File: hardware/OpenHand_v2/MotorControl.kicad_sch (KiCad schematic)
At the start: 52 parts, among them U10 DRV8833PWP, U7 DRV8833PWP, U8 DRV8833PWP, U9 DRV8833PWP

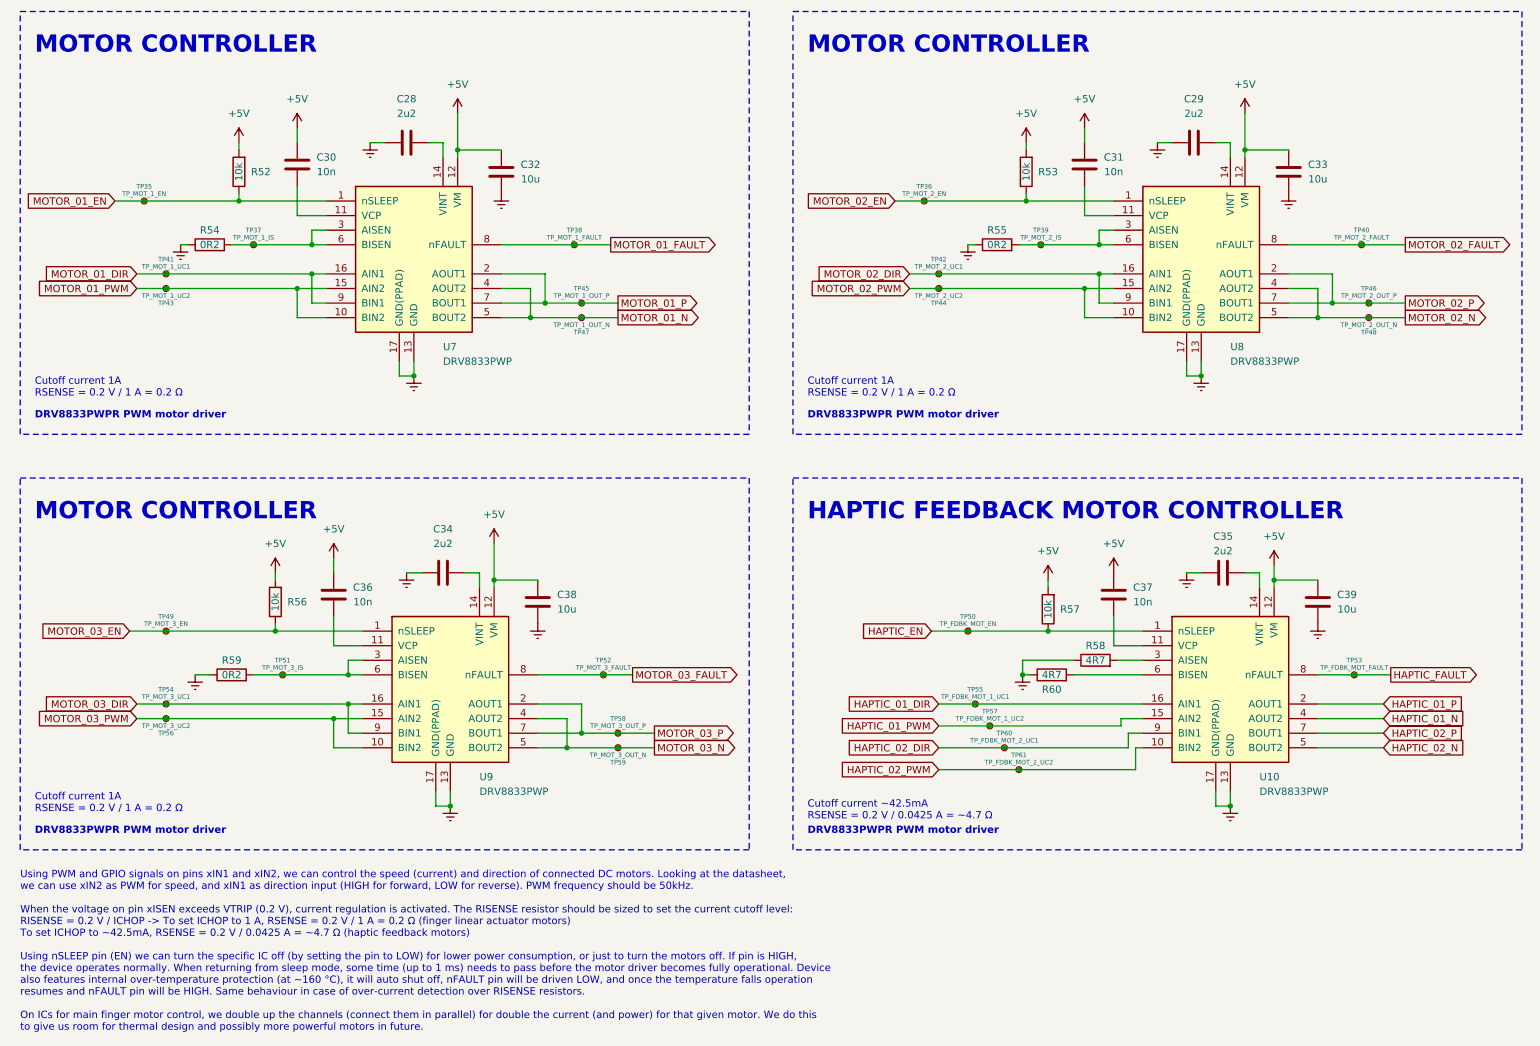
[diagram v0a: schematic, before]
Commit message: Update V2 schematic and start PCB layout
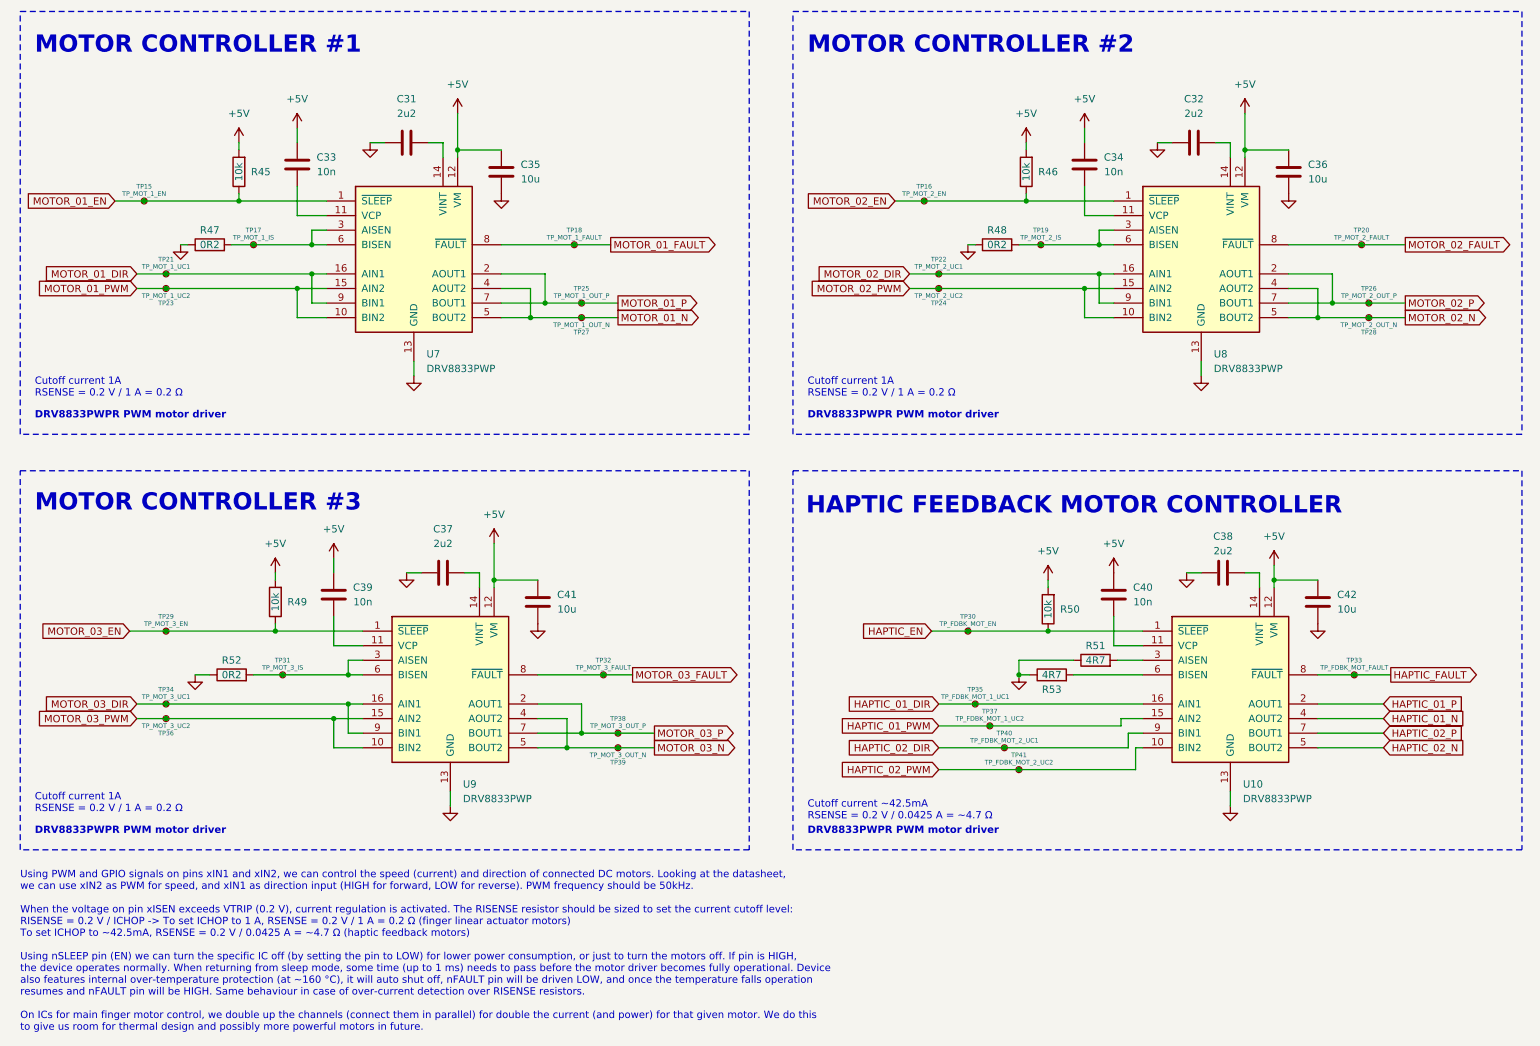
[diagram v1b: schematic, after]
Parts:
- renumbered C28 to C31, C29 to C32, C30 to C33, C31 to C34, C32 to C35, C33 to C36, C34 to C37, C35 to C38, C36 to C39, C37 to C40, C38 to C41, C39 to C42, R52 to R45, R53 to R46, R54 to R47, R55 to R48, R56 to R49, R57 to R50, R58 to R51, R59 to R52, R60 to R53, TP35 to TP15, TP36 to TP16, TP37 to TP17, TP38 to TP18, TP39 to TP19, TP40 to TP20, TP41 to TP21, TP42 to TP22, TP43 to TP23, TP44 to TP24, TP45 to TP25, TP46 to TP26, TP47 to TP27, TP48 to TP28, TP49 to TP29, TP50 to TP30, TP51 to TP31, TP52 to TP32, TP53 to TP33, TP54 to TP34, TP55 to TP35, TP56 to TP36, TP57 to TP37, TP58 to TP38, TP59 to TP39, TP60 to TP40, TP61 to TP41
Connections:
- net Earth renamed GND
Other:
- note added: "MOTOR CONTROLLER #1"
- note added: "MOTOR CONTROLLER #2"
- note added: "MOTOR CONTROLLER #3"
- note removed: "MOTOR CONTROLLER"

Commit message: Add V2 PCB and update CubeIDE config for V2
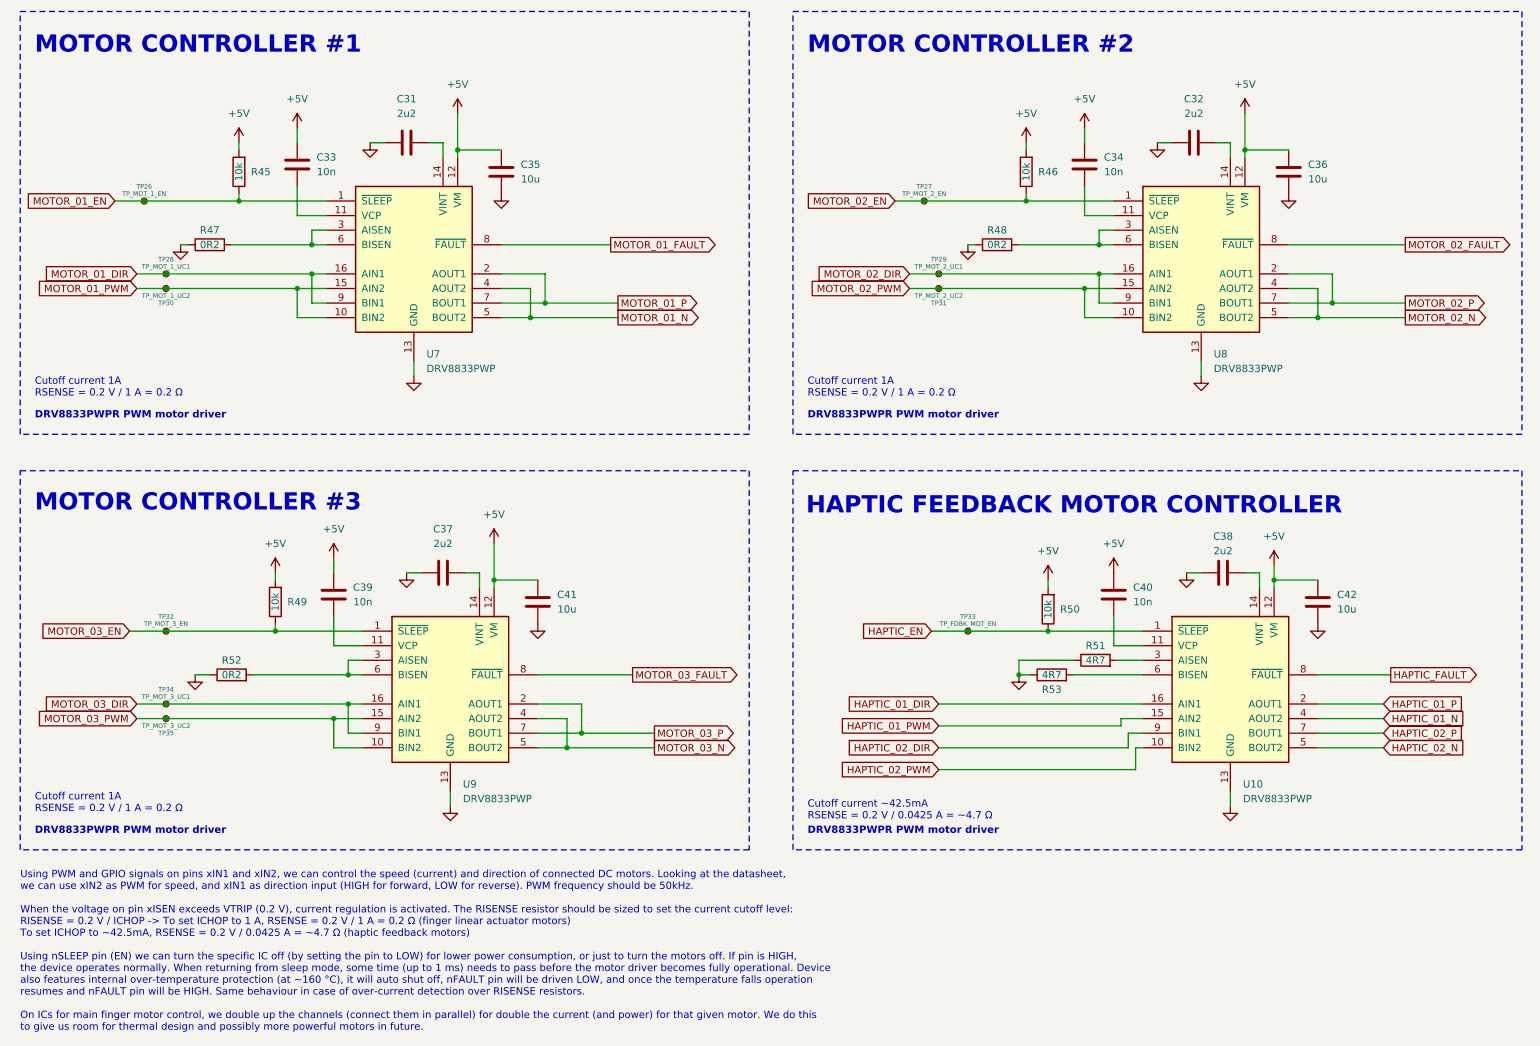
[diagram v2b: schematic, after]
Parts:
- removed TP17: TP_MOT_1_IS, TestPoint:TestPoint_Pad_D1.0mm, symbol Connector:TestPoint_Small
- removed TP18: TP_MOT_1_FAULT, TestPoint:TestPoint_Pad_D1.0mm, symbol Connector:TestPoint_Small
- removed TP19: TP_MOT_2_IS, TestPoint:TestPoint_Pad_D1.0mm, symbol Connector:TestPoint_Small
- removed TP20: TP_MOT_2_FAULT, TestPoint:TestPoint_Pad_D1.0mm, symbol Connector:TestPoint_Small
- removed TP25: TP_MOT_1_OUT_P, TestPoint:TestPoint_Pad_D1.0mm, symbol Connector:TestPoint_Small
- removed TP26: TP_MOT_2_OUT_P, TestPoint:TestPoint_Pad_D1.0mm, symbol Connector:TestPoint_Small
- removed TP27: TP_MOT_1_OUT_N, TestPoint:TestPoint_Pad_D1.0mm, symbol Connector:TestPoint_Small
- removed TP28: TP_MOT_2_OUT_N, TestPoint:TestPoint_Pad_D1.0mm, symbol Connector:TestPoint_Small
- removed TP31: TP_MOT_3_IS, TestPoint:TestPoint_Pad_D1.0mm, symbol Connector:TestPoint_Small
- removed TP32: TP_MOT_3_FAULT, TestPoint:TestPoint_Pad_D1.0mm, symbol Connector:TestPoint_Small
- removed TP33: TP_FDBK_MOT_FAULT, TestPoint:TestPoint_Pad_D1.0mm, symbol Connector:TestPoint_Small
- removed TP35: TP_FDBK_MOT_1_UC1, TestPoint:TestPoint_Pad_D1.0mm, symbol Connector:TestPoint_Small
- removed TP37: TP_FDBK_MOT_1_UC2, TestPoint:TestPoint_Pad_D1.0mm, symbol Connector:TestPoint_Small
- removed TP38: TP_MOT_3_OUT_P, TestPoint:TestPoint_Pad_D1.0mm, symbol Connector:TestPoint_Small
- removed TP39: TP_MOT_3_OUT_N, TestPoint:TestPoint_Pad_D1.0mm, symbol Connector:TestPoint_Small
- removed TP40: TP_FDBK_MOT_2_UC1, TestPoint:TestPoint_Pad_D1.0mm, symbol Connector:TestPoint_Small
- removed TP41: TP_FDBK_MOT_2_UC2, TestPoint:TestPoint_Pad_D1.0mm, symbol Connector:TestPoint_Small
- renumbered TP15 to TP26, TP16 to TP27, TP21 to TP28, TP22 to TP29, TP23 to TP30, TP24 to TP31, TP29 to TP32, TP30 to TP33, TP36 to TP35
